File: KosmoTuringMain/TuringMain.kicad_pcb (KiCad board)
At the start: 2 copper layers, 95 x 119 mm, 100 parts, among them IC1 TL072P, IC2 78L09, IC3 78L09, J2 Conn_01x10_Male, T1 2N3904, U1 TL074_

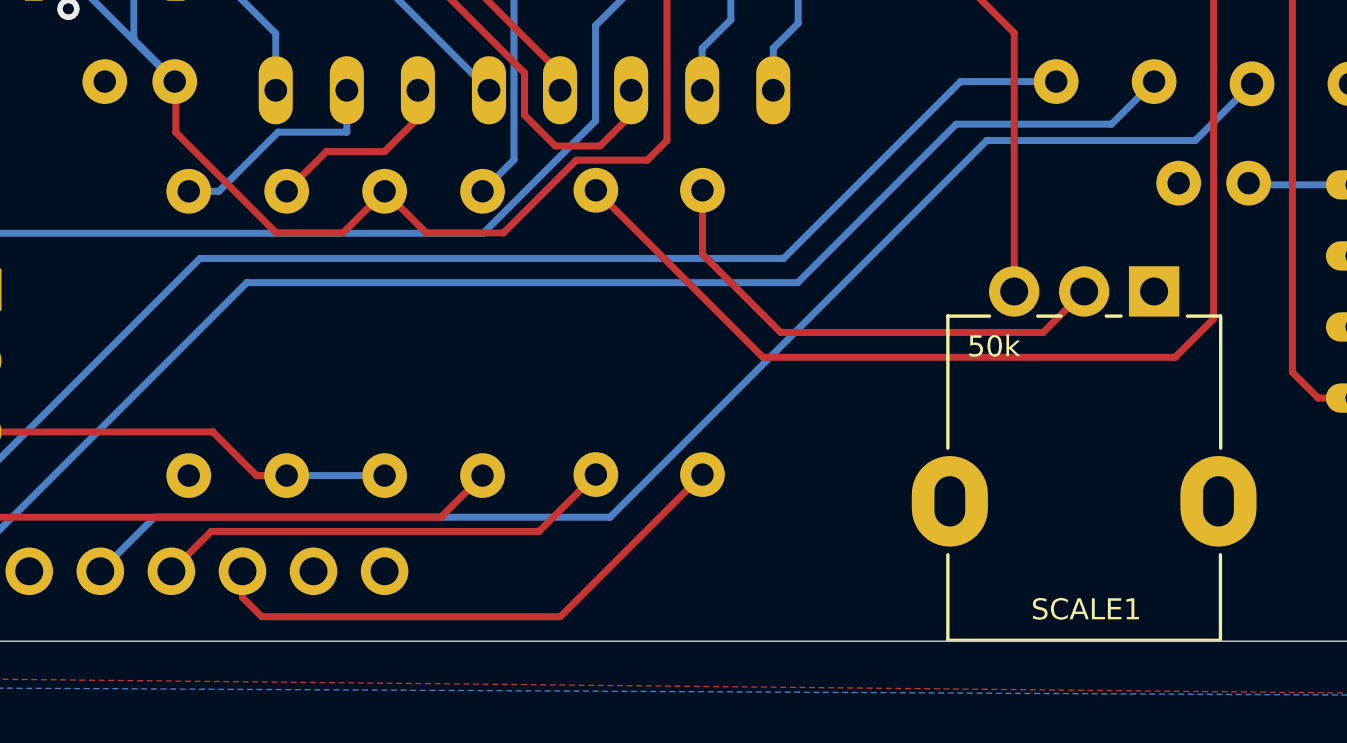
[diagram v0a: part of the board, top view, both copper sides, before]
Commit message: move pulse out 1k resistor after the led, so it does not act as voltage divider, thanks @holmesrichards !
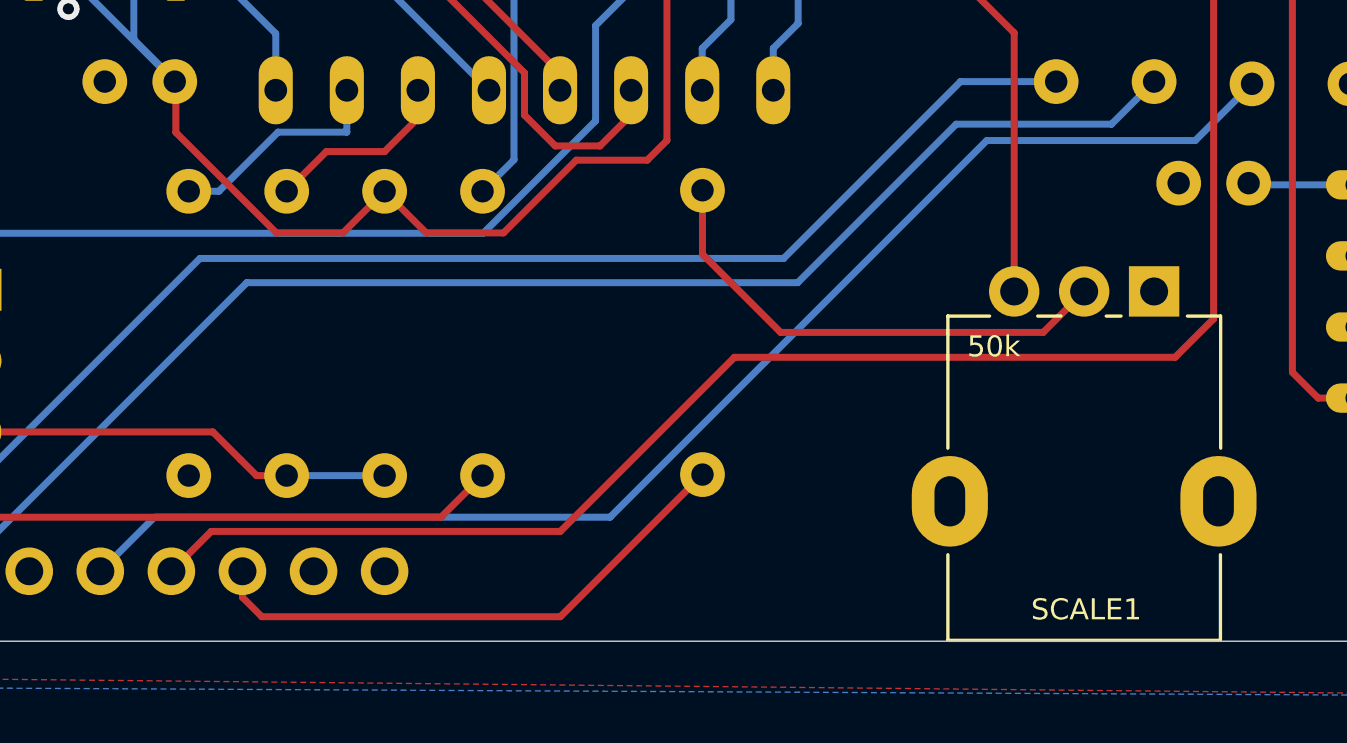
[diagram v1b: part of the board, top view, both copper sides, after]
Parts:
- removed R39: 1k, ao_tht:R_Axial_DIN0207_L6.3mm_D2.5mm_P10.16mm_Horizontal
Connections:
- BUFFER1 pad 15: Net-(BUFFER1-Pad15) -> /PULSE_OUT
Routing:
- net Net-(BUFFER1-Pad15): track 113.4 -> 0.00 mm
- net /PULSE_OUT: track 16.6 -> 129.3 mm
